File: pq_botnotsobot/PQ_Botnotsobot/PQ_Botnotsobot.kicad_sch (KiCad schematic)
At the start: 2 parts

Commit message: Functional revision and finishing touches part I
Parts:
- removed KILLSWITCH1 (x2): D2F-01L-A, SW-TH_D2F-01L, symbol Bottom_board-altium-import:0_D2F-01L-A
- added Annotation1, Annotation2, Annotation3, Annotation4: Silkscreen_Annotation, symbols-nsl:NSL_long, symbol symbols-nsl:Silkscreen_Annotation
- added Annotation5: Silkscreen_Annotation, symbols-nsl:GRSS, symbol symbols-nsl:Silkscreen_Annotation
- added Annotation6: Silkscreen_Annotation, symbols-nsl:IEEE_logo, symbol symbols-nsl:Silkscreen_Annotation
- added Annotation7: Silkscreen_Annotation, symbols-nsl:Bridgemaker, symbol symbols-nsl:Silkscreen_Annotation
- added H1, H2, H3, H4, H5, H6: MountingHole_Pad, MountingHole:MountingHole_2.2mm_M2_Pad, symbol Mechanical:MountingHole_Pad
- added J1: D2FLA, miscelaneous-nsl:D2FLA, symbol miscelaneous-nsl:D2FLA
- added J2: D2FLA1, miscelaneous-nsl:D2FLA1, symbol miscelaneous-nsl:D2FLA
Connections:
- no-connect marks 6 -> 12
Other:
- note added: "Kill Swtiches"
- note added: "Logos"
- note added: "Mounting holes"

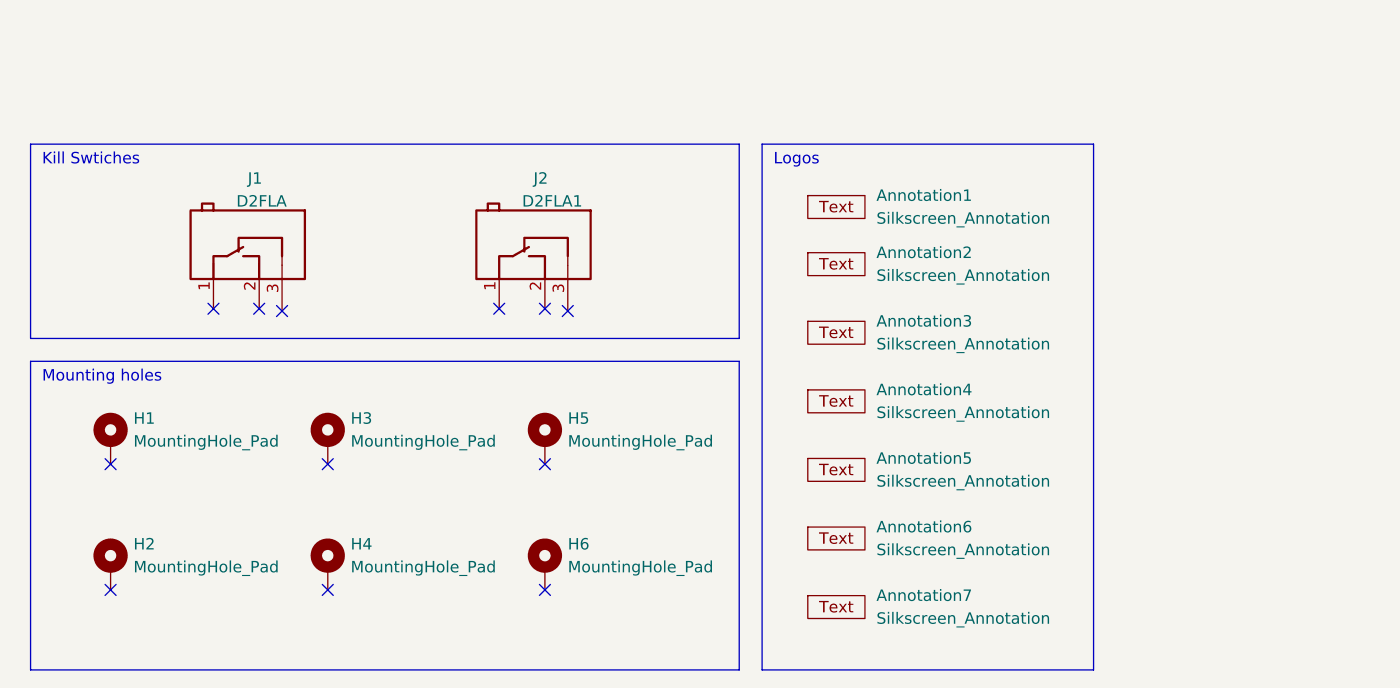
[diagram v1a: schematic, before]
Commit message: Full Kicad7 transition, library improvement and adaptation, correct footprints and 3D models added
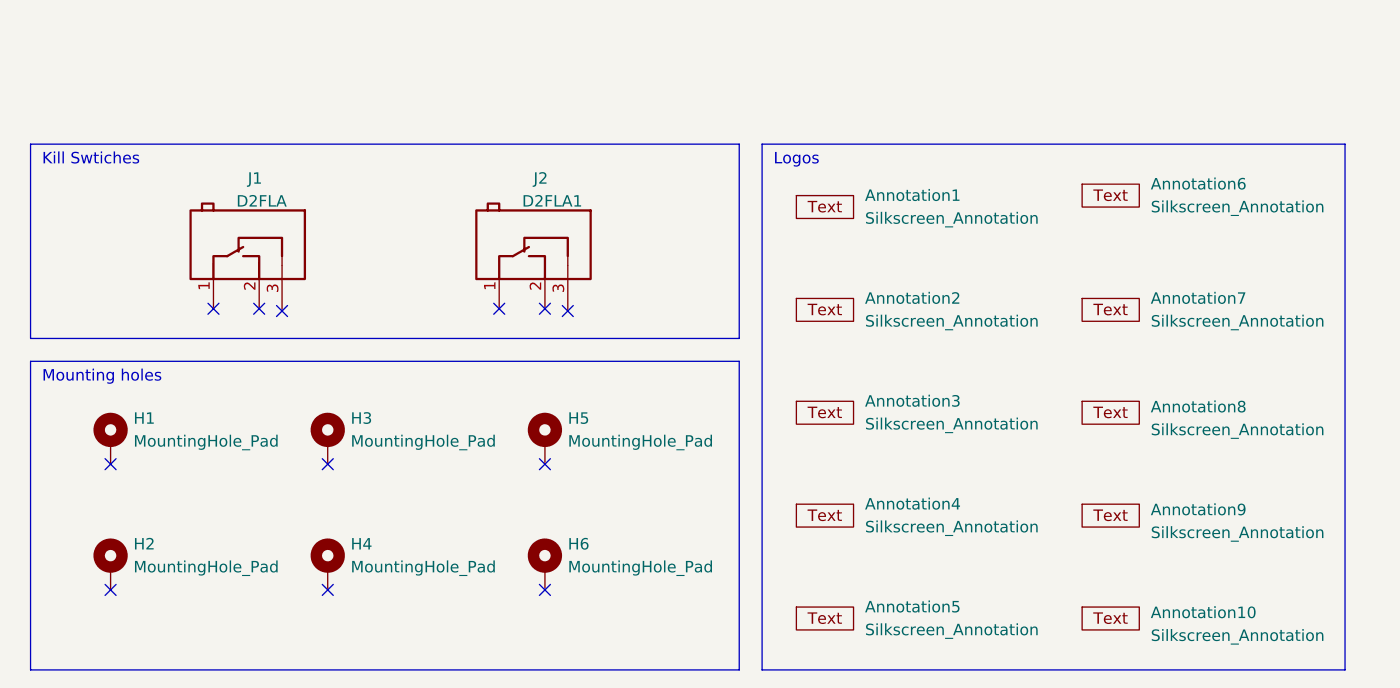
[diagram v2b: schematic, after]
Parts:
- added Annotation10: Silkscreen_Annotation, -nsl_symbols:NSL, symbol -nsl_symbols:Silkscreen_Annotation
- added Annotation8: Silkscreen_Annotation, -nsl_symbols:UPC_positiu, symbol -nsl_symbols:Silkscreen_Annotation
- added Annotation9: Silkscreen_Annotation, -nsl_symbols:Telecos, symbol -nsl_symbols:Silkscreen_Annotation
- Annotation1, Annotation2, Annotation3, Annotation4: footprint symbols-nsl:NSL_long -> -nsl_symbols:NSL_long
- Annotation5: footprint symbols-nsl:GRSS -> -nsl_symbols:GRSS
- Annotation6: footprint symbols-nsl:IEEE_logo -> -nsl_symbols:IEEE_logo
- Annotation7: footprint symbols-nsl:Bridgemaker -> -nsl_symbols:Bridgemaker
- J1: footprint miscelaneous-nsl:D2FLA -> -nsl_miscellaneous:D2FLA; now left out of the parts list
- J2: footprint miscelaneous-nsl:D2FLA1 -> -nsl_miscellaneous:D2FLA1; now left out of the parts list
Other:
- moved on the sheet: Annotation1, Annotation2, Annotation3, Annotation4, Annotation5, Annotation6, Annotation7
